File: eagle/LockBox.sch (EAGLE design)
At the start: 11 parts

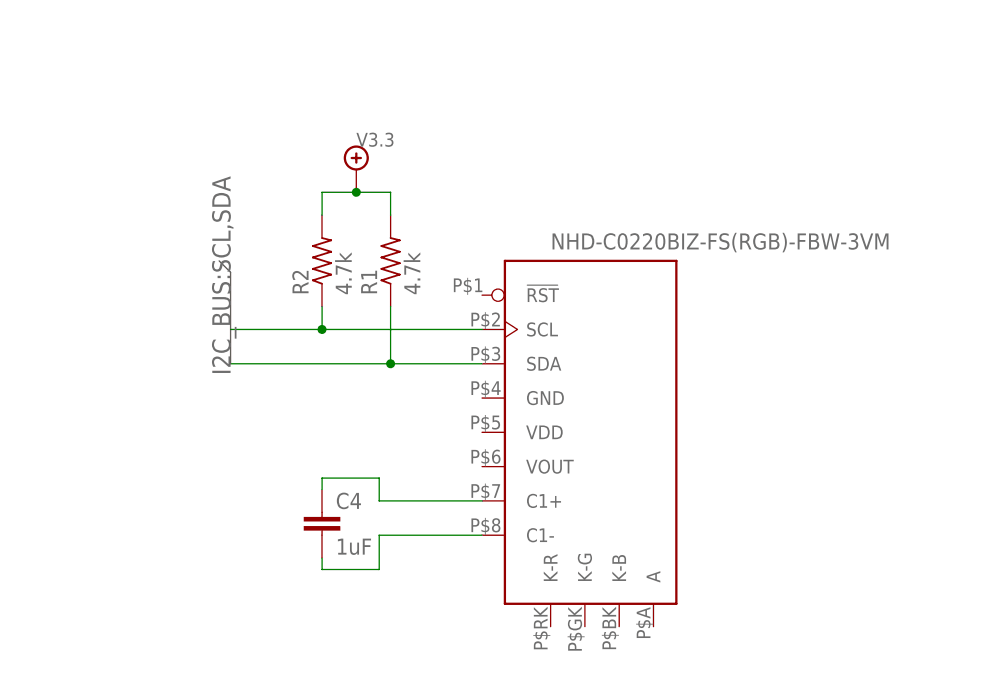
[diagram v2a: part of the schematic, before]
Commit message: Added gnd and vout connections to the LCD screen in LockBox.sch Moved pins and modified part name in LockBox.lbr.  These pins were poorly placed and were moved to allow for a cleaner schematic in LockBox.sch
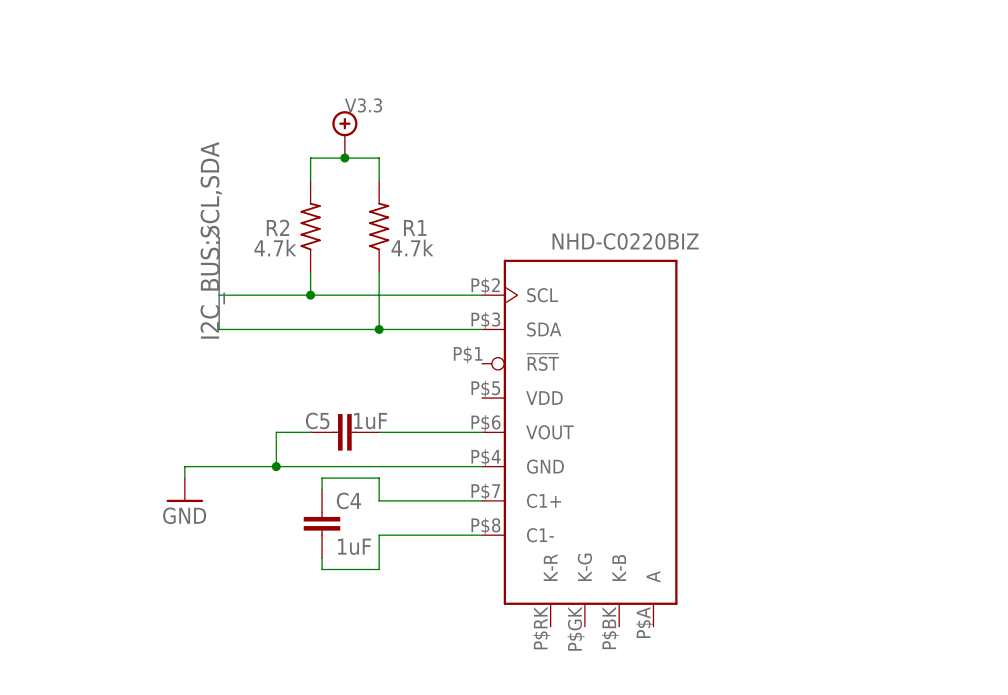
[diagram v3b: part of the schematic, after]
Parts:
- added C5: 1uF, LockBox:C
- U$5: value NHD-C0220BIZ-FS(RGB)-FBW-3VM -> NHD-C0220BIZ; device LockBox:NHD-C0220BIZ-FS(RGB)-FBW-3VM -> LockBox:NHD-C0220BIZ
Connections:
- new net N$4: C5.2, U$5.VOUT
- net GND: now also C5.1, U$5.GND
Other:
- moved on the sheet: R1, R2
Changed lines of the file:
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@@
 <part name="U$3" library="LockBox" deviceset="PJ_075" device="" technology="DH"/>
 <part name="U$4" library="LockBox" deviceset="TIP120" device=""/>
-<part name="U$5" library="LockBox" deviceset="NHD-C0220BIZ-FS(RGB)-FBW-3VM" device=""/>
 <part name="C1" library="LockBox" deviceset="C" device="" value="330pF"/>
 <part name="C2" library="LockBox" deviceset="C" device="" value="10uF"/>
@@
 <part name="R2" library="LockBox" deviceset="R-US_" device="M0805" value="4.7k"/>
 <part name="V3" library="LockBox" deviceset="V3.3" device=""/>
+<part name="GND4" library="LockBox" deviceset="GND" device=""/>
+<part name="C5" library="LockBox" deviceset="C" device="" value="1uF"/>
+<part name="U$5" library="LockBox" deviceset="NHD-C0220BIZ" device=""/>
 </parts>
 <sheets>
@@
 <instance part="U$3" gate="G$1" x="26.035" y="151.765"/>
 <instance part="U$4" gate="G$1" x="113.03" y="67.31"/>
-<instance part="U$5" gate="G$1" x="199.39" y="135.89"/>
 <instance part="C1" gate="G$1" x="41.148" y="146.812"/>
 <instance part="C2" gate="G$1" x="74.93" y="146.558"/>
@@
 <instance part="V2" gate="G1" x="21.59" y="90.17"/>
 <instance part="C4" gate="G$1" x="168.91" y="125.73"/>
-<instance part="R1" gate="G$1" x="176.53" y="153.67" rot="R90"/>
-<instance part="R2" gate="G$1" x="168.91" y="153.67" rot="R90"/>
-<instance part="V3" gate="G1" x="172.72" y="163.83"/>
+<instance part="R1" gate="G$1" x="175.26" y="157.48" smashed="yes" rot="R90">
+<attribute name="NAME" x="177.8" y="156.4386" size="1.778" layer="95"/>
+<attribute name="VALUE" x="176.53" y="154.178" size="1.778" layer="96"/>
+</instance>
+<instance part="R2" gate="G$1" x="167.64" y="157.48" smashed="yes" rot="R90">
+<attribute name="NAME" x="162.56" y="156.4386" size="1.778" layer="95"/>
+<attribute name="VALUE" x="161.29" y="154.178" size="1.778" layer="96"/>
+</instance>
+<instance part="V3" gate="G1" x="171.45" y="167.64"/>
+<instance part="GND4" gate="1" x="153.67" y="127"/>
+<instance part="C5" gate="G$1" x="170.18" y="134.62" smashed="yes" rot="R90">
+<attribute name="NAME" x="169.926" y="136.779" size="1.778" layer="95" rot="R180"/>
+<attribute name="VALUE" x="176.276" y="136.779" size="1.778" layer="96" rot="R180"/>
+</instance>
+<instance part="U$5" gate="G$1" x="199.39" y="135.89"/>
 </instances>
 <busses>
@@
 </segment>
 <segment>
-<wire x1="157.48" y1="153.67" x2="158.75" y2="152.4" width="0.762" layer="92"/>
-<wire x1="158.75" y1="152.4" x2="158.75" y2="142.24" width="0.762" layer="92"/>
-<label x="158.75" y="140.97" size="2.032" layer="95" rot="R90"/>
+<wire x1="156.21" y1="157.48" x2="157.48" y2="156.21" width="0.762" layer="92"/>
+<wire x1="157.48" y1="156.21" x2="157.48" y2="146.05" width="0.762" layer="92"/>
+<label x="157.48" y="144.78" size="2.032" layer="95" rot="R90"/>
 </segment>
 </bus>
@@
 <junction x="21.59" y="74.93"/>
 </segment>
+<segment>
+<wire x1="153.67" y1="130.81" x2="153.67" y2="129.54" width="0.1524" layer="91"/>
+<pinref part="GND4" gate="1" pin="GND"/>
+<wire x1="186.69" y1="130.81" x2="163.83" y2="130.81" width="0.1524" layer="91"/>
+<pinref part="C5" gate="G$1" pin="1"/>
+<wire x1="163.83" y1="130.81" x2="153.67" y2="130.81" width="0.1524" layer="91"/>
+<wire x1="167.64" y1="134.62" x2="163.83" y2="134.62" width="0.1524" layer="91"/>
+<wire x1="163.83" y1="134.62" x2="163.83" y2="130.81" width="0.1524" layer="91"/>
+<junction x="163.83" y="130.81"/>
+<pinref part="U$5" gate="G$1" pin="GND"/>
+</segment>
 </net>
 <net name="P$1" class="0">
@@
 <segment>
 <pinref part="R2" gate="G$1" pin="2"/>
-<wire x1="168.91" y1="158.75" x2="168.91" y2="161.29" width="0.1524" layer="91"/>
-<wire x1="168.91" y1="161.29" x2="172.72" y2="161.29" width="0.1524" layer="91"/>
+<wire x1="167.64" y1="162.56" x2="167.64" y2="165.1" width="0.1524" layer="91"/>
+<wire x1="167.64" y1="165.1" x2="171.45" y2="165.1" width="0.1524" layer="91"/>
 <pinref part="R1" gate="G$1" pin="2"/>
-<wire x1="172.72" y1="161.29" x2="176.53" y2="161.29" width="0.1524" layer="91"/>
-<wire x1="176.53" y1="161.29" x2="176.53" y2="158.75" width="0.1524" layer="91"/>
+<wire x1="171.45" y1="165.1" x2="175.26" y2="165.1" width="0.1524" layer="91"/>
+<wire x1="175.26" y1="165.1" x2="175.26" y2="162.56" width="0.1524" layer="91"/>
 <pinref part="V3" gate="G1" pin="P$1"/>
-<junction x="172.72" y="161.29"/>
+<junction x="171.45" y="165.1"/>
 </segment>
 </net>
@@
 </segment>
 <segment>
+<wire x1="157.48" y1="149.86" x2="167.64" y2="149.86" width="0.1524" layer="91"/>
+<pinref part="R2" gate="G$1" pin="1"/>
+<wire x1="167.64" y1="149.86" x2="167.64" y2="152.4" width="0.1524" layer="91"/>
+<wire x1="167.64" y1="149.86" x2="186.69" y2="149.86" width="0.1524" layer="91"/>
+<junction x="167.64" y="149.86"/>
 <pinref part="U$5" gate="G$1" pin="SCL"/>
-<wire x1="158.75" y1="146.05" x2="168.91" y2="146.05" width="0.1524" layer="91"/>
-<pinref part="R2" gate="G$1" pin="1"/>
-<wire x1="168.91" y1="146.05" x2="186.69" y2="146.05" width="0.1524" layer="91"/>
-<wire x1="168.91" y1="146.05" x2="168.91" y2="148.59" width="0.1524" layer="91"/>
-<junction x="168.91" y="146.05"/>
 </segment>
 </net>
@@
 </segment>
 <segment>
+<wire x1="157.48" y1="146.05" x2="175.26" y2="146.05" width="0.1524" layer="91"/>
+<pinref part="R1" gate="G$1" pin="1"/>
+<wire x1="175.26" y1="146.05" x2="175.26" y2="152.4" width="0.1524" layer="91"/>
+<wire x1="175.26" y1="146.05" x2="186.69" y2="146.05" width="0.1524" layer="91"/>
+<junction x="175.26" y="146.05"/>
 <pinref part="U$5" gate="G$1" pin="SDA"/>
-<wire x1="158.75" y1="142.24" x2="176.53" y2="142.24" width="0.1524" layer="91"/>
-<pinref part="R1" gate="G$1" pin="1"/>
-<wire x1="176.53" y1="142.24" x2="186.69" y2="142.24" width="0.1524" layer="91"/>
-<wire x1="176.53" y1="142.24" x2="176.53" y2="148.59" width="0.1524" layer="91"/>
-<junction x="176.53" y="142.24"/>
 </segment>
 </net>
@@
 <net name="N$2" class="0">
 <segment>
-<pinref part="U$5" gate="G$1" pin="C1+"/>
 <wire x1="186.69" y1="127" x2="175.26" y2="127" width="0.1524" layer="91"/>
 <wire x1="175.26" y1="127" x2="175.26" y2="129.54" width="0.1524" layer="91"/>
@@
 <pinref part="C4" gate="G$1" pin="1"/>
 <wire x1="168.91" y1="129.54" x2="168.91" y2="128.27" width="0.1524" layer="91"/>
+<pinref part="U$5" gate="G$1" pin="C1+"/>
 </segment>
 </net>
 <net name="N$3" class="0">
 <segment>
-<pinref part="U$5" gate="G$1" pin="C1-"/>
 <wire x1="186.69" y1="123.19" x2="175.26" y2="123.19" width="0.1524" layer="91"/>
 <wire x1="175.26" y1="123.19" x2="175.26" y2="119.38" width="0.1524" layer="91"/>
@@
 <pinref part="C4" gate="G$1" pin="2"/>
 <wire x1="168.91" y1="119.38" x2="168.91" y2="120.65" width="0.1524" layer="91"/>
-</segment>
-</net>
+<pinref part="U$5" gate="G$1" pin="C1-"/>
+</segment>
+</net>
+<net name="N$4" class="0">
+<segment>
+<pinref part="C5" gate="G$1" pin="2"/>
+<wire x1="186.69" y1="134.62" x2="175.26" y2="134.62" width="0.1524" layer="91"/>
+<pinref part="U$5" gate="G$1" pin="VOUT"/>
+</segment>
+</net>

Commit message: Added KR, KG, KB, and A connections to the LCD screen.
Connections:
- new net N$6: U$5.!RST
- net GND: now also U$5.K-B, U$5.K-G, U$5.K-R
- net P$1: now also U$5.A, U$5.VDD
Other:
- note added: "LCD Screen"
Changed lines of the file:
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@@
 <wire x1="11.43" y1="180.34" x2="91.44" y2="180.34" width="0.635" layer="97"/>
 <text x="15.24" y="173.99" size="3.81" layer="97">Power Supply - 3.3V, 1.5A LDO</text>
+<wire x1="220.98" y1="180.34" x2="220.98" y2="104.14" width="0.635" layer="97"/>
+<wire x1="220.98" y1="180.34" x2="147.32" y2="180.34" width="0.635" layer="97"/>
+<wire x1="147.32" y1="180.34" x2="147.32" y2="104.14" width="0.635" layer="97"/>
+<wire x1="147.32" y1="104.14" x2="220.98" y2="104.14" width="0.635" layer="97"/>
+<text x="170.18" y="173.99" size="3.81" layer="97">LCD Screen</text>
 </plain>
 <instances>
@@
 <junction x="163.83" y="130.81"/>
 <pinref part="U$5" gate="G$1" pin="GND"/>
+<pinref part="U$5" gate="G$1" pin="K-B"/>
+<wire x1="201.93" y1="113.03" x2="201.93" y2="109.22" width="0.1524" layer="91"/>
+<pinref part="U$5" gate="G$1" pin="K-G"/>
+<wire x1="198.12" y1="113.03" x2="198.12" y2="109.22" width="0.1524" layer="91"/>
+<pinref part="U$5" gate="G$1" pin="K-R"/>
+<wire x1="198.12" y1="109.22" x2="194.31" y2="109.22" width="0.1524" layer="91"/>
+<wire x1="194.31" y1="109.22" x2="194.31" y2="113.03" width="0.1524" layer="91"/>
+<wire x1="201.93" y1="109.22" x2="198.12" y2="109.22" width="0.1524" layer="91"/>
+<wire x1="194.31" y1="109.22" x2="163.83" y2="109.22" width="0.1524" layer="91"/>
+<wire x1="163.83" y1="109.22" x2="163.83" y2="130.81" width="0.1524" layer="91"/>
+<junction x="194.31" y="109.22"/>
+<junction x="198.12" y="109.22"/>
 </segment>
 </net>
@@
 <pinref part="V3" gate="G1" pin="P$1"/>
 <junction x="171.45" y="165.1"/>
+<pinref part="U$5" gate="G$1" pin="VDD"/>
+<wire x1="186.69" y1="138.43" x2="171.45" y2="138.43" width="0.1524" layer="91"/>
+<wire x1="171.45" y1="138.43" x2="171.45" y2="165.1" width="0.1524" layer="91"/>
+<wire x1="175.26" y1="165.1" x2="213.36" y2="165.1" width="0.1524" layer="91"/>
+<wire x1="213.36" y1="165.1" x2="213.36" y2="109.22" width="0.1524" layer="91"/>
+<wire x1="213.36" y1="109.22" x2="205.74" y2="109.22" width="0.1524" layer="91"/>
+<pinref part="U$5" gate="G$1" pin="A"/>
+<wire x1="205.74" y1="109.22" x2="205.74" y2="113.03" width="0.1524" layer="91"/>
 </segment>
 </net>
@@
 </segment>
 </net>
+<net name="N$6" class="0">
+<segment>
+<pinref part="U$5" gate="G$1" pin="!RST"/>
+<wire x1="186.69" y1="142.24" x2="151.13" y2="142.24" width="0.1524" layer="91"/>
+</segment>
+</net>
